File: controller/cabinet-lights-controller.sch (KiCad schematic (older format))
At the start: 45 parts, among them P1 CONN_01X02, P2 CONN_01X03, Q1 FDT434P, U1 NCP1077, U2 LTV-358T, U3 NCP431, U4 10k

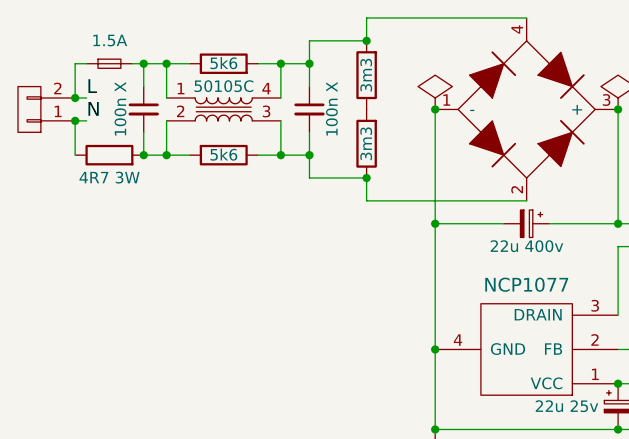
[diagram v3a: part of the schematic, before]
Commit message: Slowly adding part-nos and footprints for controller
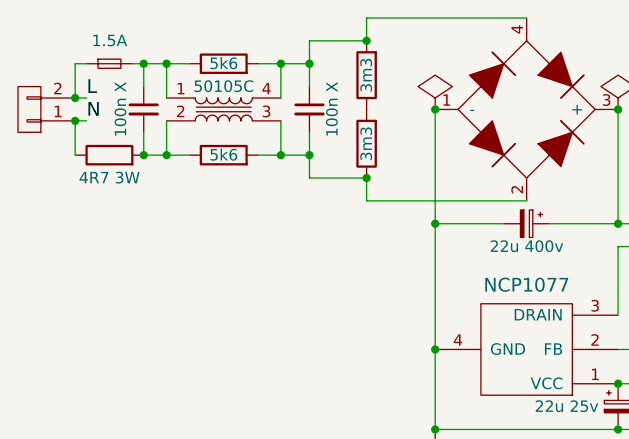
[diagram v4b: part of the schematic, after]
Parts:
- removed C2: 100n X, symbol C_Small
- removed R2: 5k6, agg:0805, symbol R
- removed R4: 3m3, agg:0805, symbol R
- added C?: 100n X, parts:B32922, symbol C_Small
- added R?: 5k6, agg:1206, symbol R
- added R?: 3m3, agg:1206, symbol R
- C1: footprint (none) -> parts:B32922; Farnell (none) -> 2315560
- C8: footprint (none) -> parts:Ceramic_Disc_Inline_7.5mm; Farnell (none) -> 1902229
- D1: footprint (none) -> parts:WOBM
- F1: footprint (none) -> parts:2410; Farnell (none) -> 1885105
- R1: footprint (none) -> parts:SM_3; Farnell (none) -> 1086378
- R3: footprint agg:0805 -> agg:1206; Farnell (none) -> 2447530
- R5: footprint agg:0805 -> agg:1206; Farnell (none) -> 2139750
- R7: footprint (none) -> agg:1206; Farnell (none) -> 2332165
- U1: Farnell (none) -> 2454531
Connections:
- net at C1.2, R1.2, TR?.2: now also R?.1
- net at D1.4, R3.2, TR?.4: now also C?.1, R?.2
- net at D1.2, R5.1, TR?.3: now also C?.2, R?.2
- net at R5.2: now also R?.1
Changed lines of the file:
@@
 F 0 "F1" H 2175 2485 50  0001 C CNN
 F 1 "1.5A" H 2175 2400 50  0000 C CNN
-F 2 "" H 2175 2300 50  0001 C CNN
-F 3 "" H 2175 2300 50  0000 C CNN
+F 2 "parts:2410" H 2175 2300 50  0001 C CNN
+F 3 "http://www.farnell.com/datasheets/1651023.pdf" H 2175 2300 50  0001 C CNN
+F 4 "1885105" H 2175 2300 60  0001 C CNN "Farnell"
 	1    2175 2300
 	1    0    0    -1
@@
 F 0 "C1" H 2417 2546 50  0001 L CNN
 F 1 "100n X" V 2225 2500 50  0000 C CNN
-F 2 "" H 2325 2500 50  0001 C CNN
-F 3 "" H 2325 2500 50  0000 C CNN
+F 2 "parts:B32922" H 2325 2500 50  0001 C CNN
+F 3 "http://www.farnell.com/datasheets/1718053.pdf" H 2325 2500 50  0001 C CNN
+F 4 "2315560" H 2325 2500 60  0001 C CNN "Farnell"
 	1    2325 2500
-	1    0    0    -1
-$EndComp
-$Comp
-L C_Small C2
-U 1 1 577A4290
-P 3050 2500
-F 0 "C2" H 3142 2546 50  0001 L CNN
-F 1 "100n X" V 3150 2500 50  0000 C CNN
-F 2 "" H 3050 2500 50  0001 C CNN
-F 3 "" H 3050 2500 50  0000 C CNN
-	1    3050 2500
 	1    0    0    -1
 $EndComp
@@
 F 0 "D1" H 4441 2546 50  0001 L CNN
 F 1 "Diode_Bridge" H 4441 2455 50  0001 L CNN
-F 2 "" H 4000 2500 50  0001 C CNN
+F 2 "parts:WOBM" H 4000 2500 50  0001 C CNN
 F 3 "http://www.farnell.com/datasheets/1441701.pdf?_ga=1.238681216.1253160071.1453215511" H 4000 2500 50  0001 C CNN
 F 4 "1861431" H 4000 2500 60  0001 C CNN "Farnell"
@@
 F 1 "NCP1077" H 4000 3269 60  0000 C CNN
 F 2 "TO_SOT_Packages_SMD:SOT-223" H 4000 3550 60  0001 C CNN
-F 3 "" H 4000 3550 60  0001 C CNN
+F 3 "http://www.farnell.com/datasheets/1863237.pdf" H 4000 3550 60  0001 C CNN
+F 4 "2454531" H 4000 3550 60  0001 C CNN "Farnell"
 	1    4000 3550
 	-1   0    0    1
@@
 F 0 "C8" H 5642 3946 50  0001 L CNN
 F 1 "1n Y1" V 5650 3900 50  0000 C CNN
-F 2 "" H 5550 3900 50  0001 C CNN
-F 3 "" H 5550 3900 50  0000 C CNN
+F 2 "parts:Ceramic_Disc_Inline_7.5mm" H 5550 3900 50  0001 C CNN
+F 3 "http://www.farnell.com/datasheets/2050153.pdf" H 5550 3900 50  0001 C CNN
+F 4 "1902229" H 5550 3900 60  0001 C CNN "Farnell"
 	1    5550 3900
 	0    1    1    0
@@
 $EndComp
 $Comp
-L R R4
-U 1 1 577B0B91
-P 3300 2350
-F 0 "R4" H 3370 2396 50  0001 L CNN
-F 1 "3m3" V 3300 2350 50  0000 C CNN
-F 2 "agg:0805" V 3230 2350 50  0001 C CNN
-F 3 "" H 3300 2350 50  0000 C CNN
-	1    3300 2350
-	-1   0    0    1
-$EndComp
-$Comp
 L R R5
 U 1 1 577B0B9C
@@
 F 0 "R5" H 3370 2696 50  0001 L CNN
 F 1 "3m3" V 3300 2650 50  0000 C CNN
-F 2 "agg:0805" V 3230 2650 50  0001 C CNN
-F 3 "" H 3300 2650 50  0000 C CNN
+F 2 "agg:1206" V 3230 2650 50  0001 C CNN
+F 3 "http://www.farnell.com/datasheets/2049244.pdf?_ga=1.215127959.1253160071.1453215511" H 3300 2650 50  0001 C CNN
+F 4 "2139750" H 3300 2650 60  0001 C CNN "Farnell"
 	1    3300 2650
 	-1   0    0    1
@@
 Connection ~ 3300 2800
 Connection ~ 3300 2200
-$Comp
-L R R2
-U 1 1 577B0D12
-P 2675 2700
-F 0 "R2" H 2745 2746 50  0001 L CNN
-F 1 "5k6" V 2675 2700 50  0000 C CNN
-F 2 "agg:0805" V 2605 2700 50  0001 C CNN
-F 3 "" H 2675 2700 50  0000 C CNN
-	1    2675 2700
-	0    1    1    0
-$EndComp
 $Comp
 L R R1
@@
 F 0 "R1" H 2245 2746 50  0001 L CNN
 F 1 "4R7 3W" V 2075 2700 50  0000 C CNN
-F 2 "" V 2105 2700 50  0001 C CNN
-F 3 "" H 2175 2700 50  0000 C CNN
+F 2 "parts:SM_3" H 2105 2700 50  0001 C CNN
+F 3 "http://www.farnell.com/datasheets/1572268.pdf" H 2175 2700 50  0001 C CNN
+F 4 "1086378" H 2175 2700 60  0001 C CNN "Farnell"
 	1    2175 2700
 	0    -1   -1   0
@@
 F 0 "R7" H 4995 3396 50  0001 L CNN
 F 1 "68k 0.5W" V 5000 3400 50  0000 C CNN
-F 2 "" V 4855 3350 50  0001 C CNN
-F 3 "" H 4925 3350 50  0000 C CNN
+F 2 "agg:1206" H 4855 3350 50  0001 C CNN
+F 3 "http://www.farnell.com/datasheets/1755795.pdf?_ga=1.242783746.1253160071.1453215511" H 4925 3350 50  0001 C CNN
+F 4 "2332165" H 4925 3350 60  0001 C CNN "Farnell"
 	1    4925 3350
 	-1   0    0    -1
@@
 F 0 "R3" H 2745 2346 50  0001 L CNN
 F 1 "5k6" V 2675 2300 50  0000 C CNN
-F 2 "agg:0805" V 2605 2300 50  0001 C CNN
-F 3 "" H 2675 2300 50  0000 C CNN
+F 2 "agg:1206" V 2605 2300 50  0001 C CNN
+F 3 "http://www.farnell.com/datasheets/1849611.pdf" H 2675 2300 50  0001 C CNN
+F 4 "2447530" H 2675 2300 60  0001 C CNN "Farnell"
 	1    2675 2300
 	0    -1   -1   0
@@
 Wire Wire Line
 	2025 2550 2025 2700
+$Comp
+L C_Small C?
+U 1 1 5784C806
+P 3050 2500
+F 0 "C?" H 3142 2546 50  0001 L CNN
+F 1 "100n X" V 3150 2500 50  0000 C CNN
+F 2 "parts:B32922" H 3050 2500 50  0001 C CNN
+F 3 "http://www.farnell.com/datasheets/1718053.pdf" H 3050 2500 50  0001 C CNN
+F 4 "2315560" H 3050 2500 60  0001 C CNN "Farnell"
+	1    3050 2500
+	1    0    0    -1
+$EndComp
+$Comp
+L R R?
+U 1 1 5784D130
+P 2675 2700
+F 0 "R?" H 2745 2746 50  0001 L CNN
+F 1 "5k6" V 2675 2700 50  0000 C CNN
+F 2 "agg:1206" V 2605 2700 50  0001 C CNN
+F 3 "http://www.farnell.com/datasheets/1849611.pdf" H 2675 2700 50  0001 C CNN
+F 4 "2447530" H 2675 2700 60  0001 C CNN "Farnell"
+	1    2675 2700
+	0    -1   -1   0
+$EndComp
+$Comp
+L R R?
+U 1 1 5784D1F2
+P 3300 2350
+F 0 "R?" H 3370 2396 50  0001 L CNN
+F 1 "3m3" V 3300 2350 50  0000 C CNN
+F 2 "agg:1206" V 3230 2350 50  0001 C CNN
+F 3 "http://www.farnell.com/datasheets/2049244.pdf?_ga=1.215127959.1253160071.1453215511" H 3300 2350 50  0001 C CNN
+F 4 "2139750" H 3300 2350 60  0001 C CNN "Farnell"
+	1    3300 2350
+	-1   0    0    1
+$EndComp
 $EndSCHEMATC
